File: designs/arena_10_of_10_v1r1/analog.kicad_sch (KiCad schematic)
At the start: 38 parts, among them J27 Conn_Coaxial, J28 Conn_Coaxial, J29 Conn_Coaxial, U83 OPA2277, U84 REF102AU, U85 MCP4725xxx-xCH, U86 OPA2277, U87 OPA2277

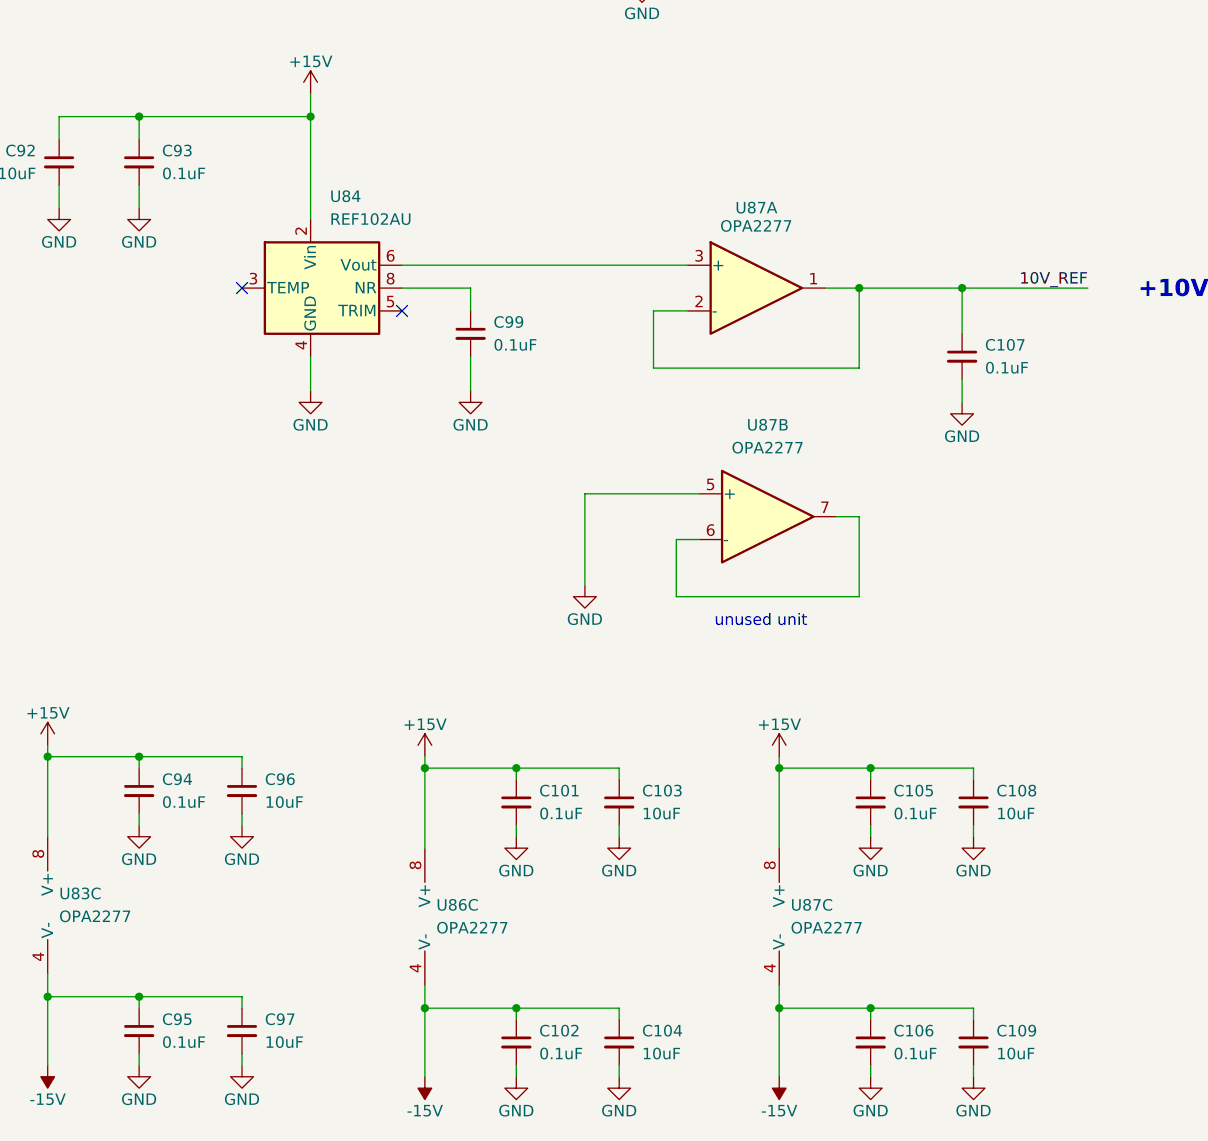
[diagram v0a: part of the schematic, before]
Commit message: Added LCSC part numbers to Symbol Fields Table.
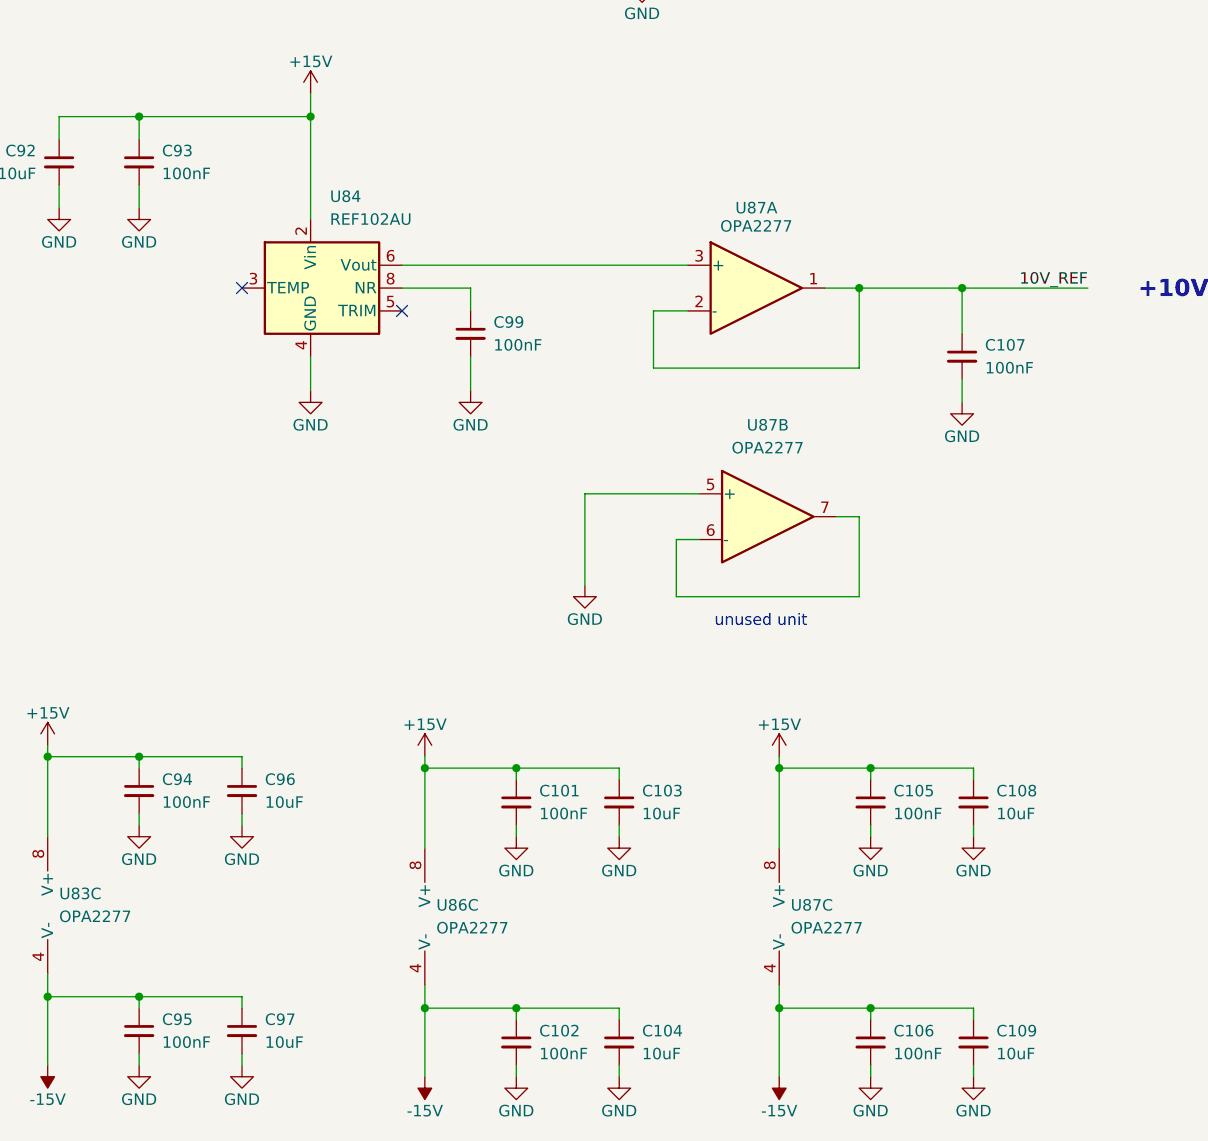
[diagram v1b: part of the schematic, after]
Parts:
- C100, C103, C104, C108, C109, C92, C96, C97: LCSC Part # (none) -> C89632
- C101, C102, C105, C106, C107, C93, C94, C95, C99: value 0.1uF -> 100nF; LCSC Part # (none) -> C307331
- C98: LCSC Part # (none) -> C1525
- D1, D2, D3, D4: LCSC Part # (none) -> C7502688
- J27, J28, J29: LCSC Part # (none) -> C2837587
- R178, R179: LCSC Part # (none) -> C705630
- R180, R181, R182, R183, R184, R185: LCSC Part # (none) -> C190095
- U83, U86, U87: LCSC Part # (none) -> C24460
- U84: LCSC Part # (none) -> C81460
- U85: LCSC Part # (none) -> C144198

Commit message: Added silkscreens.  Added required FT Rotations/Offsets for JLCPCB.
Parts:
- D1, D2, D3, D4, U85: FT Rotation Offset (none) -> 90
- J27, J28, J29: FT Rotation Offset (none) -> 180
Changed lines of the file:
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@@
 			)
 		)
+		(property "FT Rotation Offset" "90"
+			(at 158.75 109.22 0)
+			(effects
+				(font
+					(size 1.27 1.27)
+				)
+				(hide yes)
+			)
+		)
 		(pin "1"
 		)
@@
 			)
 		)
+		(property "FT Rotation Offset" "180"
+			(at 182.88 119.38 0)
+			(effects
+				(font
+					(size 1.27 1.27)
+				)
+				(hide yes)
+			)
+		)
 		(pin "2"
 		)
@@
 			)
 		)
+		(property "FT Rotation Offset" "90"
+			(at 158.75 67.31 0)
+			(effects
+				(font
+					(size 1.27 1.27)
+				)
+				(hide yes)
+			)
+		)
 		(pin "1"
 		)
@@
 			)
 		)
+		(property "FT Rotation Offset" "180"
+			(at 182.88 77.47 0)
+			(effects
+				(font
+					(size 1.27 1.27)
+				)
+				(hide yes)
+			)
+		)
 		(pin "2"
 		)
@@
 			)
 		)
+		(property "FT Rotation Offset" "90"
+			(at 60.96 74.93 0)
+			(effects
+				(font
+					(size 1.27 1.27)
+				)
+				(hide yes)
+			)
+		)
 		(pin "1"
 		)
@@
 			)
 		)
+		(property "FT Rotation Offset" "90"
+			(at 60.96 116.84 0)
+			(effects
+				(font
+					(size 1.27 1.27)
+				)
+				(hide yes)
+			)
+		)
 		(pin "1"
 		)
@@
 			)
 		)
+		(property "FT Rotation Offset" "90"
+			(at 71.12 41.91 0)
+			(effects
+				(font
+					(size 1.27 1.27)
+				)
+				(hide yes)
+			)
+		)
 		(pin "6"
 		)
@@
 			(at 105.41 41.91 0)
 			(effects
+				(font
+					(size 1.27 1.27)
+				)
+				(hide yes)
+			)
+		)
+		(property "FT Rotation Offset" "180"
+			(at 105.41 41.91 0)
+			(effects
